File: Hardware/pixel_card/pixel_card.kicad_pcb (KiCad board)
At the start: 2 copper layers, 88.9 x 50.8 mm, 0 parts

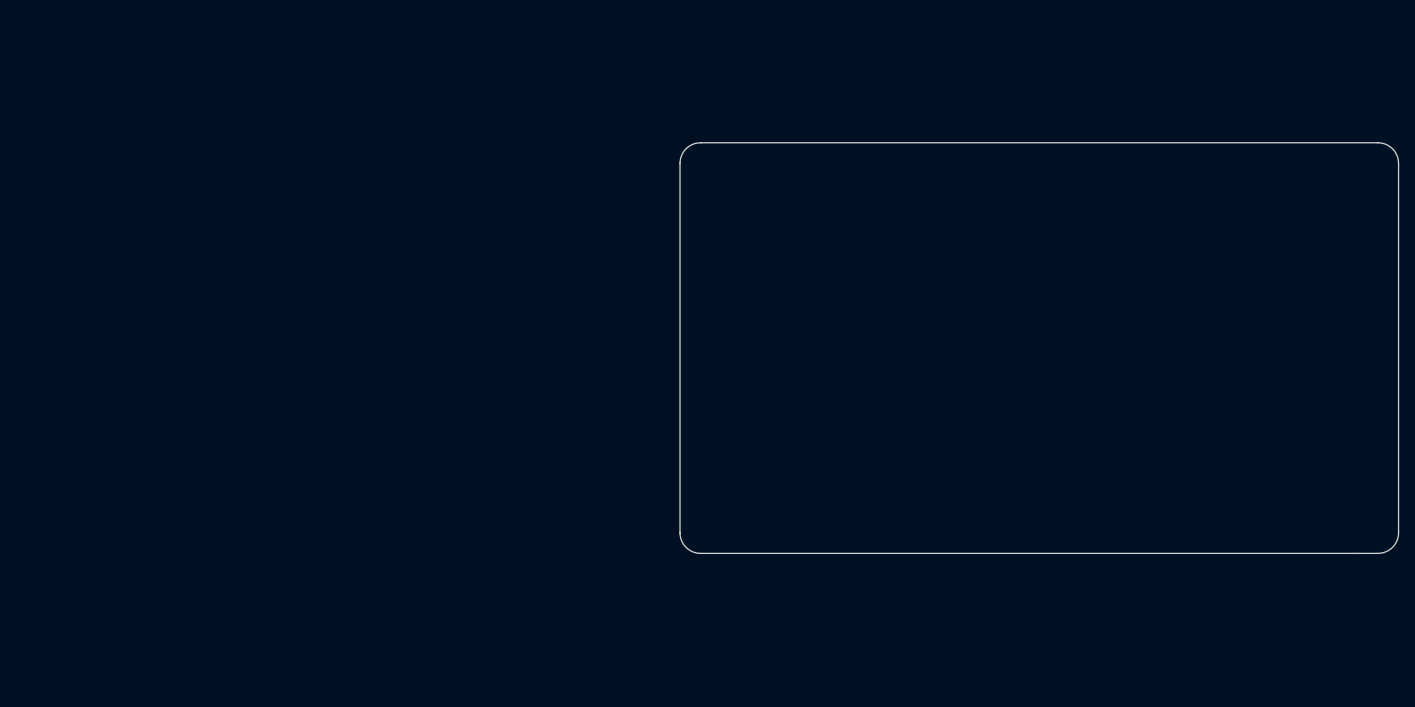
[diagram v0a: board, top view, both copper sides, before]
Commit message: Fixing schematic and mocing to pcb
1. Adding not-connected pin symbols
2. Adding footprints
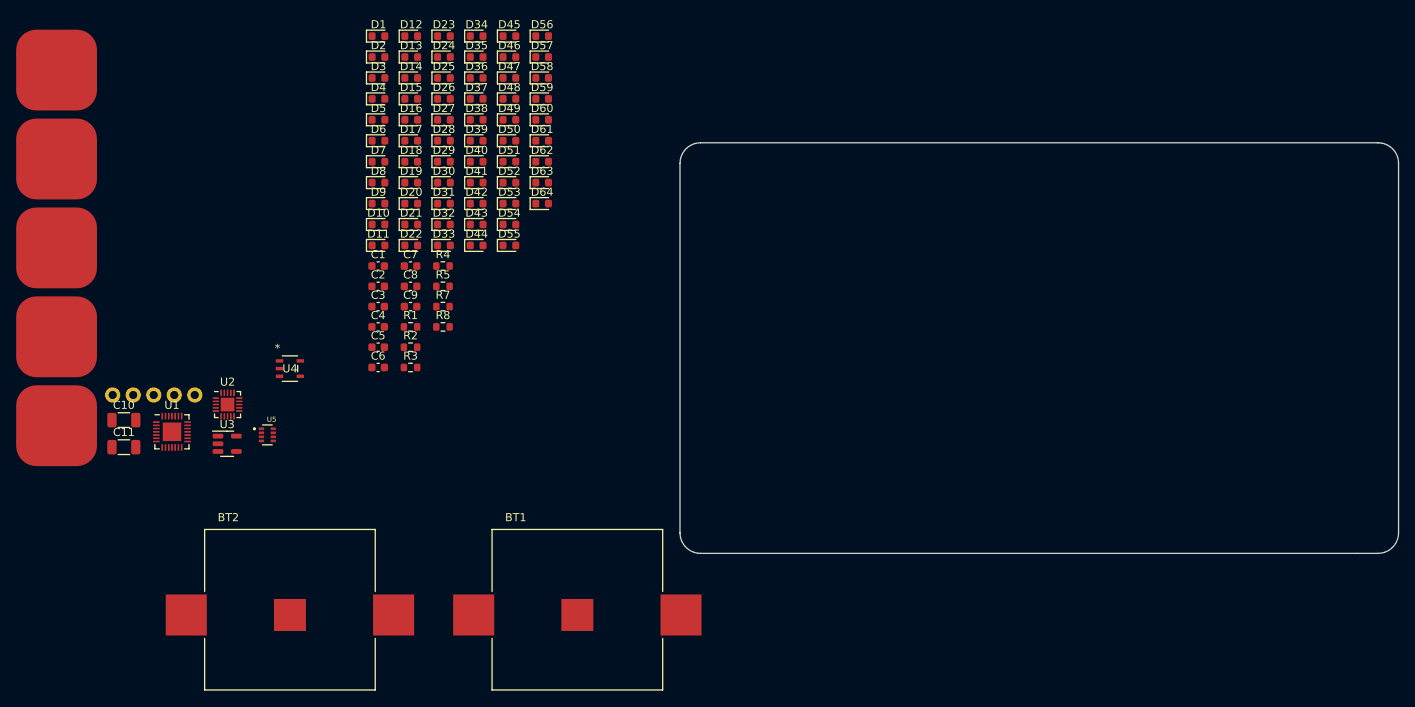
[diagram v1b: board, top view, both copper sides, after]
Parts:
- added BT1: 3002, Keystone 3002:BAT_3002, F.Cu at (91.4, 116.8)
- added BT2: 3002, Keystone 3002:BAT_3002, F.Cu at (55.9, 116.8)
- added C1: 10uF, Capacitor_SMD:C_0603_1608Metric, F.Cu at (66.8, 73.7)
- added C10: 330uF, Capacitor_SMD:C_1206_3216Metric, F.Cu at (35.3, 92.7)
- added C11: 330uF, Capacitor_SMD:C_1206_3216Metric, F.Cu at (35.3, 96.1)
- added C2: 10uF, Capacitor_SMD:C_0603_1608Metric, F.Cu at (66.8, 76.2)
- added C3: 0.1uF, Capacitor_SMD:C_0603_1608Metric, F.Cu at (66.8, 78.7)
- added C4: 0.1uF, Capacitor_SMD:C_0603_1608Metric, F.Cu at (66.8, 81.2)
- added C5: 0.1uF, Capacitor_SMD:C_0603_1608Metric, F.Cu at (66.8, 83.7)
- added C6: 1uF, Capacitor_SMD:C_0603_1608Metric, F.Cu at (66.8, 86.2)
- added C7: 1uF, Capacitor_SMD:C_0603_1608Metric, F.Cu at (70.8, 73.7)
- added C8: 1uF, Capacitor_SMD:C_0603_1608Metric, F.Cu at (70.8, 76.2)
- added C9: 1uF, Capacitor_SMD:C_0603_1608Metric, F.Cu at (70.8, 78.7)
- added D1: LED, LED_SMD:LED_0603_1608Metric, F.Cu at (66.8, 45.2)
- added D10: LED, LED_SMD:LED_0603_1608Metric, F.Cu at (66.8, 68.5)
- added D11: LED, LED_SMD:LED_0603_1608Metric, F.Cu at (66.8, 71.1)
- added D12: LED, LED_SMD:LED_0603_1608Metric, F.Cu at (70.9, 45.2)
- added D13: LED, LED_SMD:LED_0603_1608Metric, F.Cu at (70.9, 47.8)
- added D14: LED, LED_SMD:LED_0603_1608Metric, F.Cu at (70.9, 50.4)
- added D15: LED, LED_SMD:LED_0603_1608Metric, F.Cu at (70.9, 53.0)
- added D16: LED, LED_SMD:LED_0603_1608Metric, F.Cu at (70.9, 55.6)
- added D17: LED, LED_SMD:LED_0603_1608Metric, F.Cu at (70.9, 58.2)
- added D18: LED, LED_SMD:LED_0603_1608Metric, F.Cu at (70.9, 60.8)
- added D19: LED, LED_SMD:LED_0603_1608Metric, F.Cu at (70.9, 63.4)
- added D2: LED, LED_SMD:LED_0603_1608Metric, F.Cu at (66.8, 47.8)
- added D20: LED, LED_SMD:LED_0603_1608Metric, F.Cu at (70.9, 65.9)
- added D21: LED, LED_SMD:LED_0603_1608Metric, F.Cu at (70.9, 68.5)
- added D22: LED, LED_SMD:LED_0603_1608Metric, F.Cu at (70.9, 71.1)
- added D23: LED, LED_SMD:LED_0603_1608Metric, F.Cu at (74.9, 45.2)
- added D24: LED, LED_SMD:LED_0603_1608Metric, F.Cu at (74.9, 47.8)
- added D25: LED, LED_SMD:LED_0603_1608Metric, F.Cu at (74.9, 50.4)
- added D26: LED, LED_SMD:LED_0603_1608Metric, F.Cu at (74.9, 53.0)
- added D27: LED, LED_SMD:LED_0603_1608Metric, F.Cu at (74.9, 55.6)
- added D28: LED, LED_SMD:LED_0603_1608Metric, F.Cu at (74.9, 58.2)
- added D29: LED, LED_SMD:LED_0603_1608Metric, F.Cu at (74.9, 60.8)
- added D3: LED, LED_SMD:LED_0603_1608Metric, F.Cu at (66.8, 50.4)
- added D30: LED, LED_SMD:LED_0603_1608Metric, F.Cu at (74.9, 63.4)
- added D31: LED, LED_SMD:LED_0603_1608Metric, F.Cu at (74.9, 65.9)
- added D32: LED, LED_SMD:LED_0603_1608Metric, F.Cu at (74.9, 68.5)
- added D33: LED, LED_SMD:LED_0603_1608Metric, F.Cu at (74.9, 71.1)
- added D34: LED, LED_SMD:LED_0603_1608Metric, F.Cu at (79.0, 45.2)
- added D35: LED, LED_SMD:LED_0603_1608Metric, F.Cu at (79.0, 47.8)
- added D36: LED, LED_SMD:LED_0603_1608Metric, F.Cu at (79.0, 50.4)
- added D37: LED, LED_SMD:LED_0603_1608Metric, F.Cu at (79.0, 53.0)
- added D38: LED, LED_SMD:LED_0603_1608Metric, F.Cu at (79.0, 55.6)
- added D39: LED, LED_SMD:LED_0603_1608Metric, F.Cu at (79.0, 58.2)
- added D4: LED, LED_SMD:LED_0603_1608Metric, F.Cu at (66.8, 53.0)
- added D40: LED, LED_SMD:LED_0603_1608Metric, F.Cu at (79.0, 60.8)
- added D41: LED, LED_SMD:LED_0603_1608Metric, F.Cu at (79.0, 63.4)
- added D42: LED, LED_SMD:LED_0603_1608Metric, F.Cu at (79.0, 65.9)
- added D43: LED, LED_SMD:LED_0603_1608Metric, F.Cu at (79.0, 68.5)
- added D44: LED, LED_SMD:LED_0603_1608Metric, F.Cu at (79.0, 71.1)
- added D45: LED, LED_SMD:LED_0603_1608Metric, F.Cu at (83.0, 45.2)
- added D46: LED, LED_SMD:LED_0603_1608Metric, F.Cu at (83.0, 47.8)
- added D47: LED, LED_SMD:LED_0603_1608Metric, F.Cu at (83.0, 50.4)
- added D48: LED, LED_SMD:LED_0603_1608Metric, F.Cu at (83.0, 53.0)
- added D49: LED, LED_SMD:LED_0603_1608Metric, F.Cu at (83.0, 55.6)
- added D5: LED, LED_SMD:LED_0603_1608Metric, F.Cu at (66.8, 55.6)
- added D50: LED, LED_SMD:LED_0603_1608Metric, F.Cu at (83.0, 58.2)
- added D51: LED, LED_SMD:LED_0603_1608Metric, F.Cu at (83.0, 60.8)
- added D52: LED, LED_SMD:LED_0603_1608Metric, F.Cu at (83.0, 63.4)
- added D53: LED, LED_SMD:LED_0603_1608Metric, F.Cu at (83.0, 65.9)
- added D54: LED, LED_SMD:LED_0603_1608Metric, F.Cu at (83.0, 68.5)
- added D55: LED, LED_SMD:LED_0603_1608Metric, F.Cu at (83.0, 71.1)
- added D56: LED, LED_SMD:LED_0603_1608Metric, F.Cu at (87.1, 45.2)
- added D57: LED, LED_SMD:LED_0603_1608Metric, F.Cu at (87.1, 47.8)
- added D58: LED, LED_SMD:LED_0603_1608Metric, F.Cu at (87.1, 50.4)
- added D59: LED, LED_SMD:LED_0603_1608Metric, F.Cu at (87.1, 53.0)
- added D6: LED, LED_SMD:LED_0603_1608Metric, F.Cu at (66.8, 58.2)
- added D60: LED, LED_SMD:LED_0603_1608Metric, F.Cu at (87.1, 55.6)
- added D61: LED, LED_SMD:LED_0603_1608Metric, F.Cu at (87.1, 58.2)
- added D62: LED, LED_SMD:LED_0603_1608Metric, F.Cu at (87.1, 60.8)
- added D63: LED, LED_SMD:LED_0603_1608Metric, F.Cu at (87.1, 63.4)
- added D64: LED, LED_SMD:LED_0603_1608Metric, F.Cu at (87.1, 65.9)
- added D7: LED, LED_SMD:LED_0603_1608Metric, F.Cu at (66.8, 60.8)
- added D8: LED, LED_SMD:LED_0603_1608Metric, F.Cu at (66.8, 63.4)
- added D9: LED, LED_SMD:LED_0603_1608Metric, F.Cu at (66.8, 65.9)
- added J2: DEBUG, SparkFun-Connector:1X05, F.Cu at (33.9, 89.6)
- added R1: 10k, Resistor_SMD:R_0603_1608Metric, F.Cu at (70.8, 81.2)
- added R2: 10k, Resistor_SMD:R_0603_1608Metric, F.Cu at (70.8, 83.7)
- added R3: 10k, Resistor_SMD:R_0603_1608Metric, F.Cu at (70.8, 86.2)
- added R4: 10k, Resistor_SMD:R_0603_1608Metric, F.Cu at (74.8, 73.7)
- added R5: 20k, Resistor_SMD:R_0603_1608Metric, F.Cu at (74.8, 76.2)
- added R7: 50R, Resistor_SMD:R_0603_1608Metric, F.Cu at (74.8, 78.7)
- added R8: 50R, Resistor_SMD:R_0603_1608Metric, F.Cu at (74.8, 81.2)
- added SW1: UP, SparkFun-Switch:Button-CapacitiveTouch, F.Cu at (27.0, 49.4)
- added SW2: DOWN, SparkFun-Switch:Button-CapacitiveTouch, F.Cu at (27.0, 60.4)
- added SW3: LEFT, SparkFun-Switch:Button-CapacitiveTouch, F.Cu at (27.0, 71.4)
- added SW4: RIGTH, SparkFun-Switch:Button-CapacitiveTouch, F.Cu at (27.0, 82.4)
- added SW5: ACTION, SparkFun-Switch:Button-CapacitiveTouch, F.Cu at (27.0, 93.4)
- added U1: IS31FL3731-QF, Package_DFN_QFN:QFN-28-1EP_4x4mm_P0.4mm_EP2.3x2.3mm, F.Cu at (41.3, 94.2)
- added U2: ATtiny1616-M, Package_DFN_QFN:VQFN-20-1EP_3x3mm_P0.4mm_EP1.7x1.7mm, F.Cu at (48.2, 90.8)
- added U3: AP2127K-3.0, Package_TO_SOT_SMD:SOT-23-5, F.Cu at (48.1, 95.7)
- added U4: XC6210B182MR-G, XC6210B182MR-G:SOT-25_TOR, F.Cu at (55.9, 86.4)
- added U5: TPS2116DRLR, TPS2116DRLR:SOTFL50P160X60-8N, F.Cu at (53.1, 94.6)
